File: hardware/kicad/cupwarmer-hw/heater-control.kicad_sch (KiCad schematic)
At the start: 8 parts, among them Q1 AO3400 SOT-23

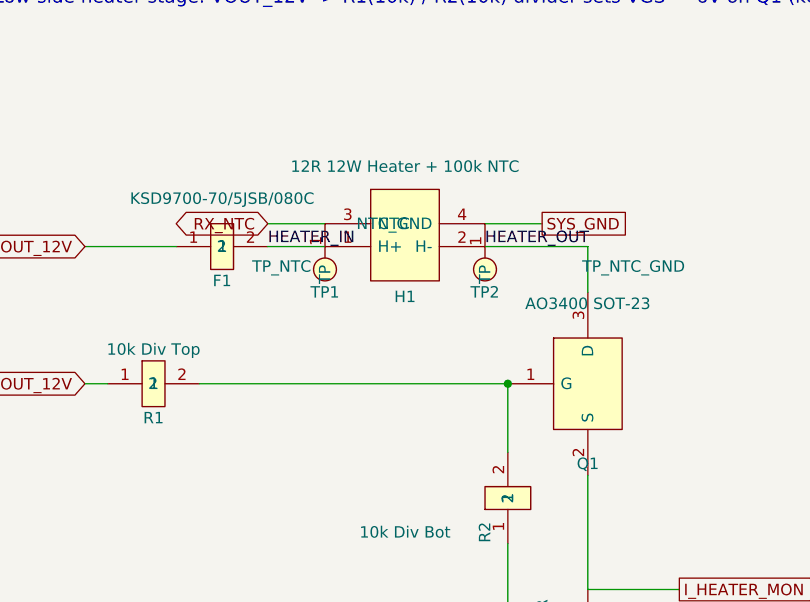
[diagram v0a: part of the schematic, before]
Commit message: Lay out H1 heater harness as 1x4 inline connector
Redraw HEATER_HARNESS_4 symbol as a horizontal 1x4 with pins ordered
H+, NTC, NTC_GND, H- to match the heater harness physical lead
sequence for hand-soldering. Renumber pins (1=H+, 2=NTC, 3=NTC_GND,
4=H-) and rebuild the footprint as an inline 4-pad row at 5 mm pitch
with 1.4 mm holes for H+/H- and 1.0 mm holes for the NTC pair.
Schematic ERC clean; PCB H1 needs Update-from-Schematic to relink
nets and reposition.

Co-Authored-By: Claude Opus 4.7 (1M context) <noreply@anthropic.com>
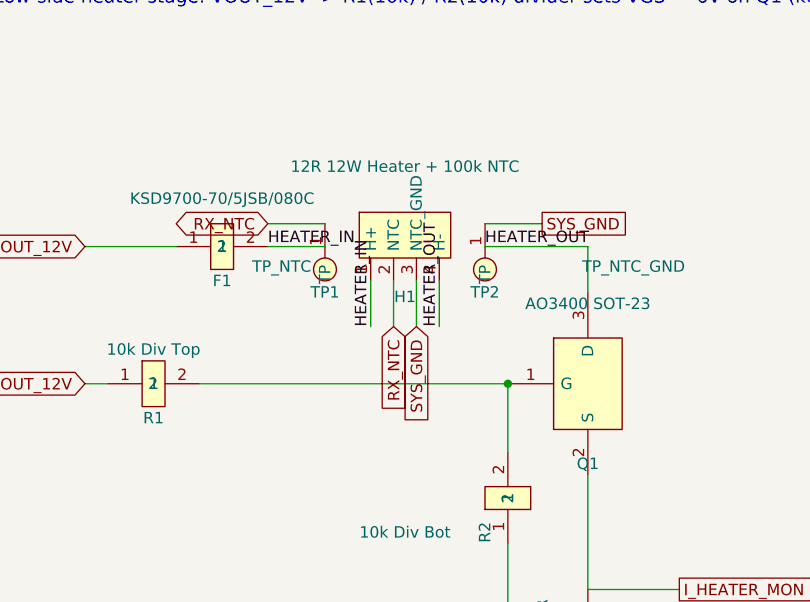
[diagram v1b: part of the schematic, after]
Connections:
- net HEATER_OUT: now also H1.4 (H-); no longer H1.2 (H-)
- net RX_NTC: now also H1.2 (NTC); no longer H1.3 (NTC)
- net SYS_GND: now also H1.3 (NTC_GND); no longer H1.4 (NTC_GND)
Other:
- moved on the sheet: H1
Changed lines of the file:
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@@
+	(wire
+		(pts
+			(xy 96.52 58.42) (xy 96.52 63.5)
+		)
+		(stroke
+			(width 0)
+			(type solid)
+		)
+	)
+	(wire
+		(pts
+			(xy 96.52 83.82) (xy 96.52 96.52)
+		)
+		(stroke
+			(width 0)
+			(type solid)
+		)
+	)
+	(wire
+		(pts
+			(xy 87.63 73.66) (xy 87.63 81.28)
+		)
+		(stroke
+			(width 0)
+			(type solid)
+		)
+	)
+	(wire
+		(pts
+			(xy 96.52 106.68) (xy 96.52 111.76)
+		)
+		(stroke
+			(width 0)
+			(type solid)
+		)
+	)
+	(wire
+		(pts
+			(xy 96.52 96.52) (xy 106.68 96.52)
+		)
+		(stroke
+			(width 0)
+			(type solid)
+		)
+	)
+	(wire
+		(pts
+			(xy 53.34 73.66) (xy 87.63 73.66)
+		)
+		(stroke
+			(width 0)
+			(type solid)
+		)
+	)
+	(wire
+		(pts
+			(xy 87.63 91.44) (xy 87.63 111.76)
+		)
+		(stroke
+			(width 0)
+			(type solid)
+		)
+	)
+	(wire
+		(pts
+			(xy 87.63 111.76) (xy 96.52 111.76)
+		)
+		(stroke
+			(width 0)
+			(type solid)
+		)
+	)
 	(wire
 		(pts
@@
 		(stroke
 			(width 0)
-			(type solid)
+			(type default)
 		)
 	)
@@
 		(stroke
 			(width 0)
-			(type solid)
-		)
-	)
-	(wire
-		(pts
-			(xy 96.52 58.42) (xy 96.52 63.5)
-		)
-		(stroke
-			(width 0)
-			(type solid)
+			(type default)
 		)
 	)
@@
 		(stroke
 			(width 0)
-			(type solid)
+			(type default)
 		)
 	)
@@
 		(stroke
 			(width 0)
-			(type solid)
-		)
-	)
-	(wire
-		(pts
-			(xy 96.52 83.82) (xy 96.52 96.52)
-		)
-		(stroke
-			(width 0)
-			(type solid)
-		)
-	)
-	(wire
-		(pts
-			(xy 87.63 73.66) (xy 87.63 81.28)
-		)
-		(stroke
-			(width 0)
-			(type solid)
-		)
-	)
-	(wire
-		(pts
-			(xy 96.52 106.68) (xy 96.52 111.76)
-		)
-		(stroke
-			(width 0)
-			(type solid)
-		)
-	)
-	(wire
-		(pts
-			(xy 96.52 96.52) (xy 106.68 96.52)
-		)
-		(stroke
-			(width 0)
-			(type solid)
-		)
-	)
-	(wire
-		(pts
-			(xy 53.34 73.66) (xy 87.63 73.66)
-		)
-		(stroke
-			(width 0)
-			(type solid)
-		)
-	)
-	(wire
-		(pts
-			(xy 87.63 91.44) (xy 87.63 111.76)
-		)
-		(stroke
-			(width 0)
-			(type solid)
-		)
-	)
-	(wire
-		(pts
-			(xy 87.63 111.76) (xy 96.52 111.76)
-		)
-		(stroke
-			(width 0)
-			(type solid)
+			(type default)
+		)
+	)
+	(wire
+		(pts
+			(xy 72.39 62.23) (xy 72.39 67.31)
+		)
+		(stroke
+			(width 0)
+			(type default)
+		)
+	)
+	(wire
+		(pts
+			(xy 74.93 62.23) (xy 74.93 67.31)
+		)
+		(stroke
+			(width 0)
+			(type default)
+		)
+	)
+	(wire
+		(pts
+			(xy 77.47 62.23) (xy 77.47 67.31)
+		)
+		(stroke
+			(width 0)
+			(type default)
+		)
+	)
+	(wire
+		(pts
+			(xy 80.01 62.23) (xy 80.01 67.31)
+		)
+		(stroke
+			(width 0)
+			(type default)
 		)
 	)
 	(label "HEATER_OUT"
 		(at 85.09 58.42 0)
+		(effects
+			(font
+				(size 1.27 1.27)
+			)
+			(justify left bottom)
+		)
+	)
+	(label "HEATER_OUT"
+		(at 80.01 67.31 270)
+		(effects
+			(font
+				(size 1.27 1.27)
+			)
+			(justify left bottom)
+		)
+	)
+	(label "HEATER_IN"
+		(at 72.39 67.31 270)
 		(effects
 			(font
@@
 			(hide yes)
 			(show_name no)
+			(do_not_autoplace no)
+			(effects
+				(font
+					(size 1.27 1.27)
+				)
+			)
+		)
+	)
+	(global_label "SYS_GND"
+		(shape input)
+		(at 77.47 67.31 270)
+		(effects
+			(font
+				(size 1.27 1.27)
+			)
+			(justify right)
+		)
+		(property "Intersheetrefs" "${INTERSHEET_REFS}"
+			(at 77.47 67.31 0)
+			(hide yes)
+			(show_name no)
+			(do_not_autoplace no)
+			(effects
+				(font
+					(size 1.27 1.27)
+				)
+			)
+		)
+	)
+	(global_label "RX_NTC"
+		(shape input)
+		(at 74.93 67.31 270)
+		(effects
+			(font
+				(size 1.27 1.27)
+			)
+			(justify right)
+		)
+		(property "Intersheetrefs" "${INTERSHEET_REFS}"
+			(at 74.93 67.31 0)
+			(hide yes)
+			(show_name no)

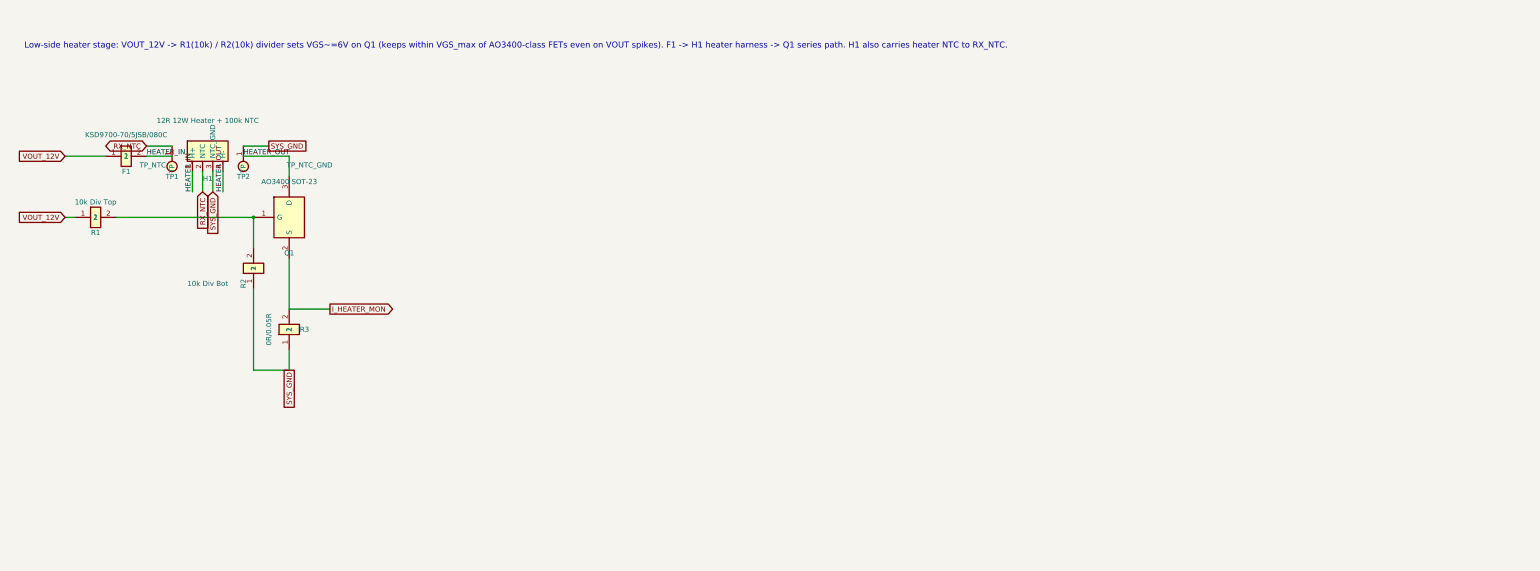
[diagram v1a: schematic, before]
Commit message: Tidy heater-control sheet layout
Drop collisions to 0 by relocating H1 + TP1/TP2 into a separate
block, lengthening pin stubs so HEATER_IN/RX_NTC/SYS_GND/HEATER_OUT
labels clear the H1 symbol body, and merging TP2 into the existing
SYS_GND rail. ERC parity preserved; total score 6476 to 2525.

Co-Authored-By: Claude Opus 4.7 (1M context) <noreply@anthropic.com>
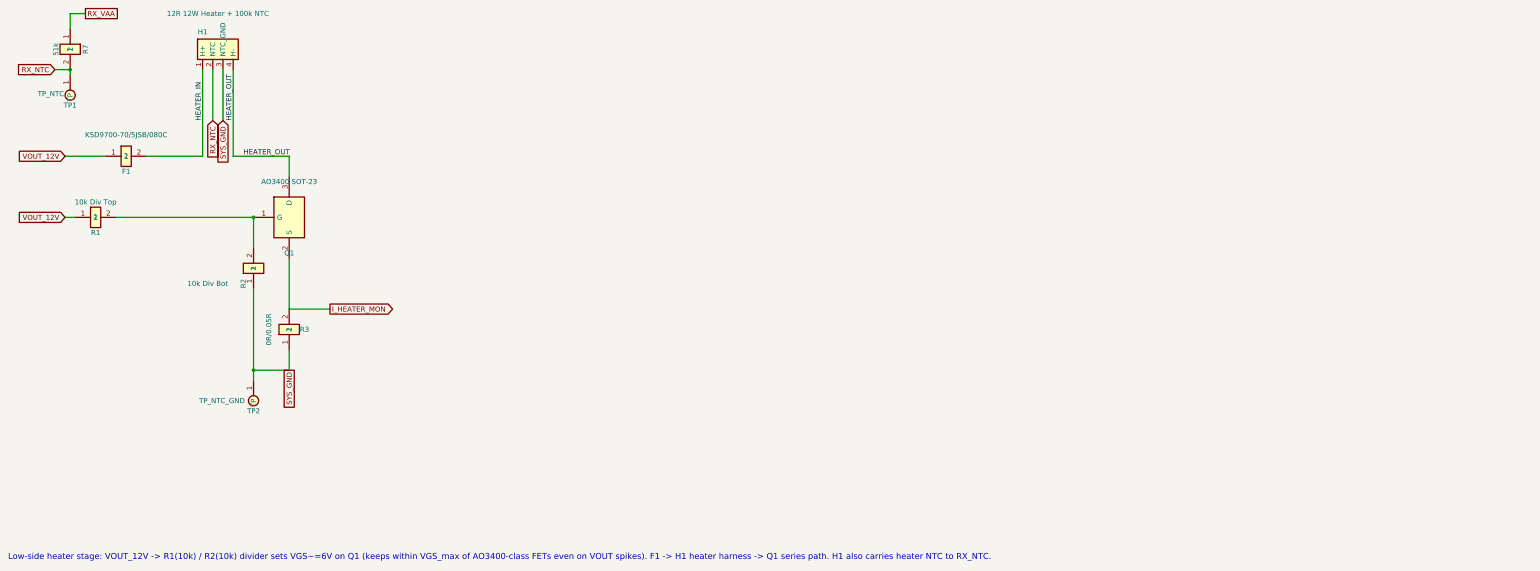
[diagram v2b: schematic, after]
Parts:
- added R7: 51k, Resistor_SMD:R_0603_1608Metric, symbol cupwarmer:PASSIVE_2
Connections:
- net RX_NTC: now also R7.2
- new net RX_VAA: R7.1
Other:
- moved on the sheet: H1, TP1, TP2

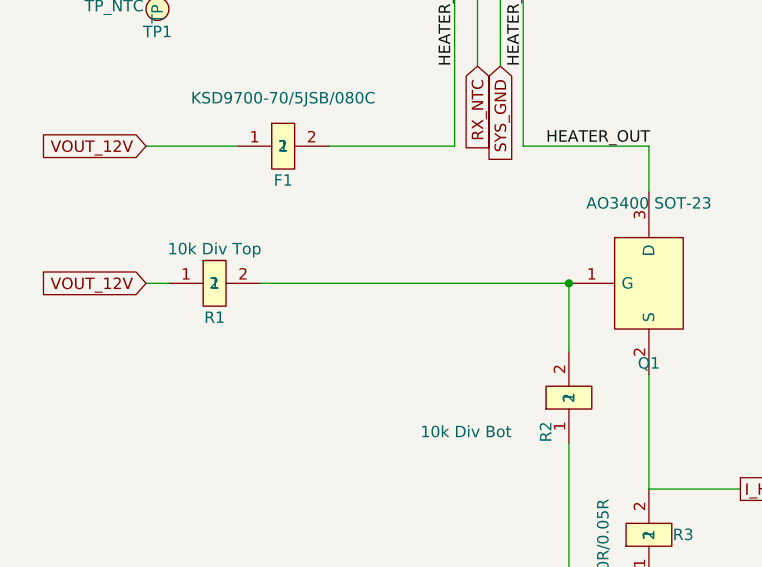
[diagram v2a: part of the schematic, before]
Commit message: Remove R7 from rx-power after move to heater-control
R7 was relocated to the heater-control sheet in 7f9c5df; clean up
the rx-power side by deleting the symbol, the now-unused junction
and wire stub, and re-anchoring the RX_VAA / RX_NTC global labels.

Co-Authored-By: Claude Opus 4.7 (1M context) <noreply@anthropic.com>
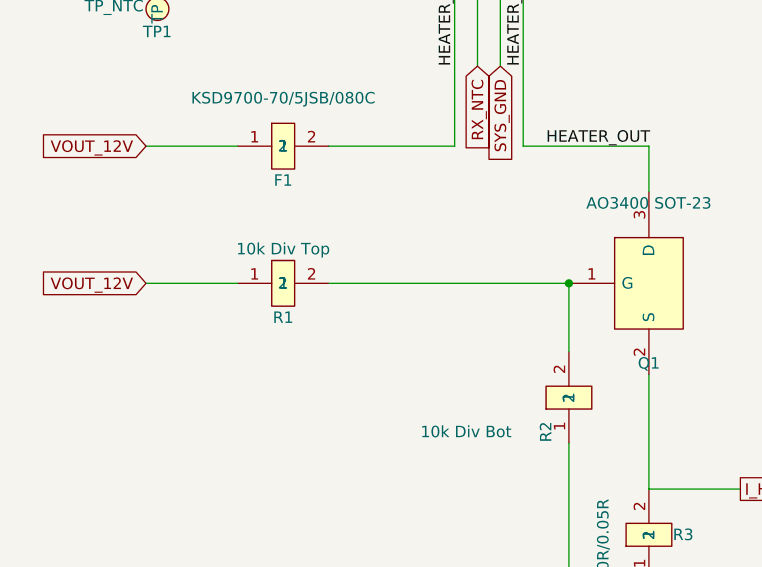
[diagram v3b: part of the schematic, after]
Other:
- moved on the sheet: R1
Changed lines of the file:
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@@
+	)
+	(junction
+		(at 87.63 111.76)
+		(diameter 0)
+		(color 0 0 0 0)
+	)
+	(junction
+		(at 41.91 36.83)
+		(diameter 0)
+		(color 0 0 0 0)
 	)
 	(junction
@@
 		(color 0 0 0 0)
 	)
-	(junction
-		(at 87.63 111.76)
-		(diameter 0)
-		(color 0 0 0 0)
-	)
-	(junction
-		(at 41.91 36.83)
-		(diameter 0)
-		(color 0 0 0 0)
-	)
 	(wire
 		(pts
@@
 	(wire
 		(pts
-			(xy 40.64 73.66) (xy 43.18 73.66)
+			(xy 40.64 73.66) (xy 50.8 73.66)
 		)
 		(stroke
@@
 	(wire
 		(pts
-			(xy 53.34 73.66) (xy 87.63 73.66)
+			(xy 60.96 73.66) (xy 87.63 73.66)
 		)
 		(stroke
@@
 	(symbol
 		(lib_id "cupwarmer:PASSIVE_2")
-		(at 48.26 73.66 0)
+		(at 55.88 73.66 0)
 		(unit 1)
 		(body_style 1)
@@
 		(dnp no)
 		(property "Reference" "R1"
-			(at 48.26 77.47 0)
+			(at 55.88 77.47 0)
 			(show_name no)
 			(do_not_autoplace no)
@@
 		)
 		(property "Value" "10k Div Top"
-			(at 48.26 69.85 0)
+			(at 55.88 69.85 0)
 			(show_name no)
 			(do_not_autoplace no)
@@
 		)
 		(property "Footprint" "Resistor_SMD:R_0603_1608Metric"
-			(at 48.26 73.66 0)
+			(at 55.88 73.66 0)
 			(hide yes)
 			(show_name no)
@@
 		)
 		(property "Datasheet" "~"
-			(at 48.26 73.66 0)
+			(at 55.88 73.66 0)
 			(hide yes)
 			(show_name no)
@@
 		)
 		(property "Description" "Gate divider top (VOUT_12V -> Q1.G)"
-			(at 48.26 73.66 0)
+			(at 55.88 73.66 0)
 			(hide yes)
 			(show_name no)
@@
 		)
 		(property "Manufacturer" "UNI-ROYAL"
-			(at 0 0 0)
+			(at 7.62 0 0)
 			(hide yes)
 			(show_name no)
@@
 		)
 		(property "LCSC" "C25804"
-			(at 0 0 0)
+			(at 7.62 0 0)
 			(hide yes)
 			(show_name no)
@@
 		)
 		(property "MPN" "0603WAF1002T5E"
-			(at 0 0 0)
-			(hide yes)
-			(show_name no)
+			(at 7.62 0 0)
+			(hide yes)
+			(show_name no)

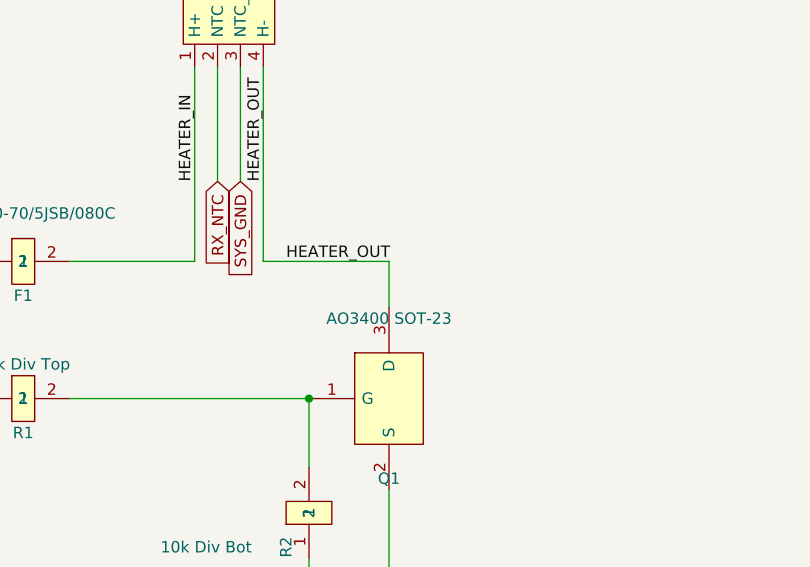
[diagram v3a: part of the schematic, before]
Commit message: Add TH2 NTC symbol to heater-control as off-board
Represents the 100k B4260 NTC physically embedded in the H1 silicone
heater harness. Symbol uses cupwarmer:PASSIVE_2 with on_board=no and
empty Footprint so it is excluded from netlist/PCB while staying
visible in the schematic. Pins tie to the existing RX_NTC and
SYS_GND nets via global labels at the pin endpoints.

Co-Authored-By: Claude Opus 4.7 (1M context) <noreply@anthropic.com>
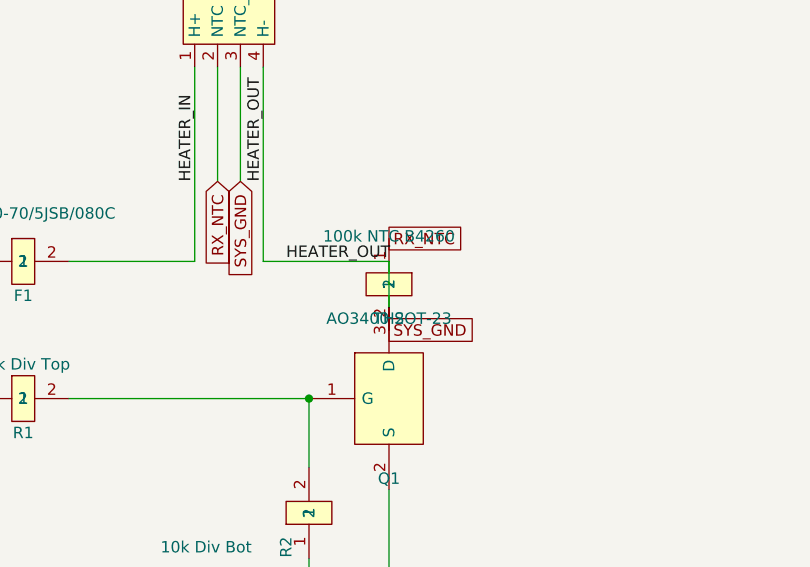
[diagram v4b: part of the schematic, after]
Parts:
- added TH2: 100k NTC B4260, symbol cupwarmer:PASSIVE_2
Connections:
- net RX_NTC: now also TH2.1
- net SYS_GND: now also TH2.2
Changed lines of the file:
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@@
+		)
+	)
+	(global_label "SYS_GND"
+		(shape passive)
+		(at 96.52 66.04 0)
+		(effects
+			(font
+				(size 1.27 1.27)
+			)
+			(justify left)
+		)
+		(property "Intersheetrefs" "${INTERSHEET_REFS}"
+			(at 96.52 66.04 0)
+			(hide yes)
+			(show_name no)
+			(do_not_autoplace no)
+			(effects
+				(font
+					(size 1.27 1.27)
+				)
+			)
+		)
+	)
+	(global_label "RX_NTC"
+		(shape passive)
+		(at 96.52 55.88 0)
+		(effects
+			(font
+				(size 1.27 1.27)
+			)
+			(justify left)
+		)
+		(property "Intersheetrefs" "${INTERSHEET_REFS}"
+			(at 96.52 55.88 0)
+			(hide yes)
+			(show_name no)
+			(do_not_autoplace no)
+			(effects
+				(font
+					(size 1.27 1.27)
+				)
+			)
 		)
 	)
@@
 					(unit 1)
 				)
+			)
+		)
+	)
+	(symbol
+		(lib_id "cupwarmer:PASSIVE_2")
+		(at 96.52 60.96 270)
+		(unit 1)
+		(body_style 1)
+		(exclude_from_sim no)
+		(in_bom yes)
+		(on_board no)
+		(in_pos_files yes)
+		(dnp no)
+		(property "Reference" "TH2"
+			(at 96.52 64.77 270)
+			(show_name no)
+			(do_not_autoplace no)
+			(effects
+				(font
+					(size 1.27 1.27)
+				)
+			)
+		)
+		(property "Value" "100k NTC B4260"
+			(at 96.52 55.626 270)
+			(show_name no)
+			(do_not_autoplace no)
+			(effects
+				(font
+					(size 1.27 1.27)
+				)
+			)
+		)
+		(property "Footprint" ""
+			(at 96.52 60.96 270)
+			(hide yes)
+			(show_name no)
+			(do_not_autoplace no)
+			(effects
+				(font
+					(size 1.27 1.27)
+				)
+			)
+		)
+		(property "Datasheet" "~"
+			(at 96.52 60.96 270)
+			(hide yes)
+			(show_name no)
+			(do_not_autoplace no)
+			(effects
+				(font
+					(size 1.27 1.27)
+				)
+			)
+		)
+		(property "Description" "Heater-embedded 100k NTC thermistor (B=4260); physically inside H1 harness, off-board"
+			(at 96.52 60.96 270)
+			(hide yes)
+			(show_name no)
+			(do_not_autoplace no)
+			(effects
+				(font
+					(size 1.27 1.27)
+				)
+			)
+		)
+		(property "Manufacturer" ""
+			(at 0 0 0)
+			(hide yes)
+			(show_name no)
+			(do_not_autoplace no)
+			(effects
+				(font
+					(size 1.27 1.27)
+				)
+			)
+		)
+		(property "LCSC" ""
+			(at 0 0 0)
+			(hide yes)
+			(show_name no)
+			(do_not_autoplace no)
+			(effects
+				(font
+					(size 1.27 1.27)
+				)
+			)
+		)
+		(property "MPN" ""
+			(at 0 0 0)
+			(hide yes)
+			(show_name no)
+			(do_not_autoplace no)
+			(effects
+				(font
+					(size 1.27 1.27)
+				)
+			)
+		)
+		(pin "1"
+		)
+		(pin "2"
+		)
+		(instances
+			(project "cupwarmer-hw"
+				(path "/f3c63676-f392-4700-9f58-a6787e1eb284/22222222-2222-2222-2222-222222222222"
+					(reference "TH2")
+					(unit 1)
+				)
